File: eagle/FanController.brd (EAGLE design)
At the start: 45 x 20 mm, 16 parts, among them IC102 LDK320AM33R, IC201 STM32F042G6U6, Q302 BSS123

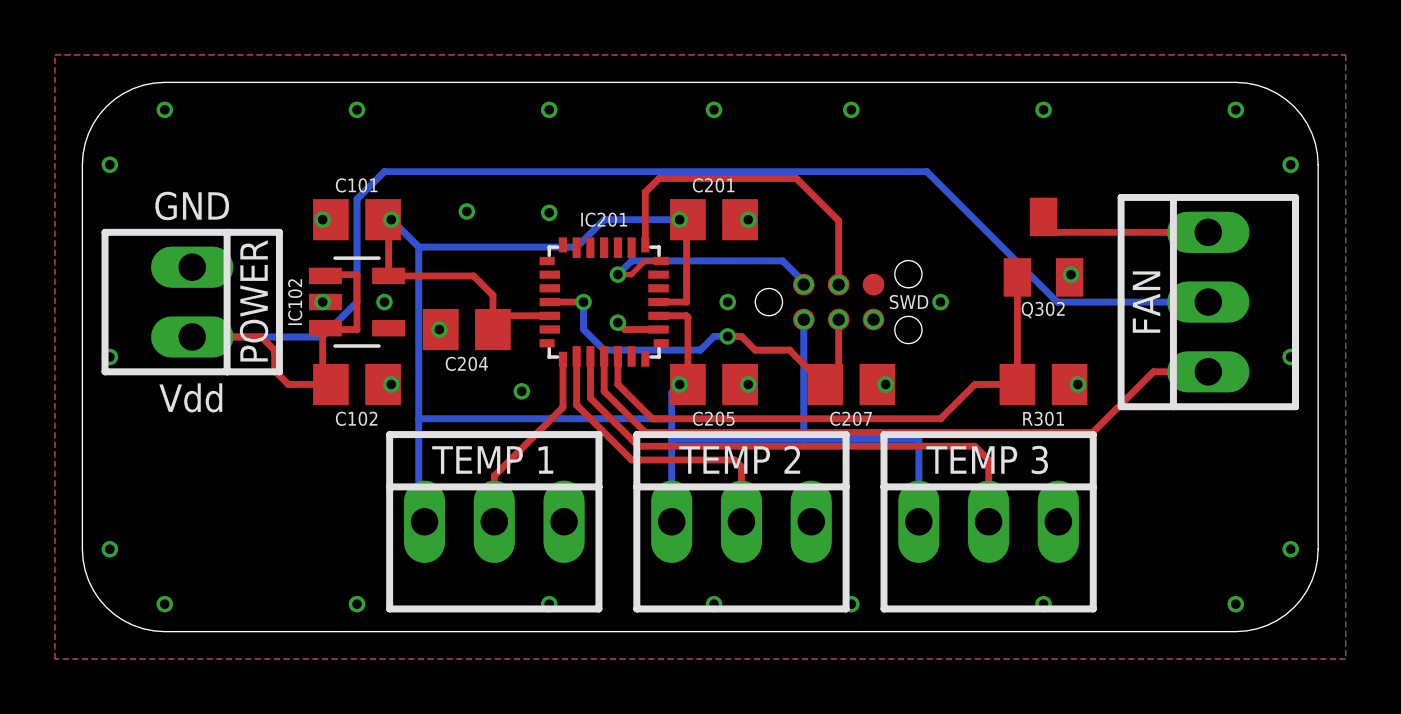
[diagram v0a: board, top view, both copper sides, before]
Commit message: rev.2: PWM fan
- initialized all unused pins as analog
- replaced 3-pin fan connector with 4-pin
- removed FET for transistor control
- added noctua PWM specification white paper
- rev.2 board marking on tstop
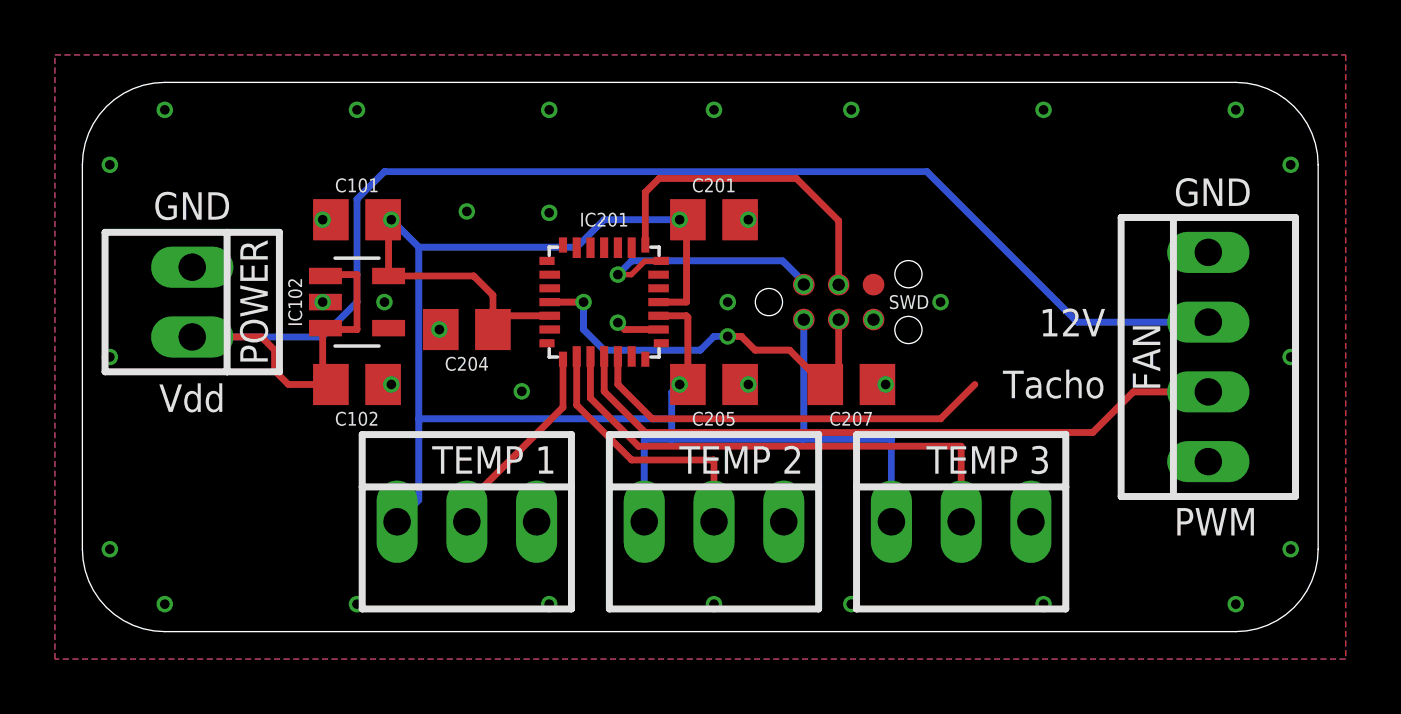
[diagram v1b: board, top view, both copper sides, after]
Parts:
- removed FAN_300: 22-23-2031, con-molex:22-23-2031
- removed Q302: BSS123, transistor-small-signal:SOT23
- removed R301: 10k, rcl:R0805
- added FAN_301: 47053-1000, con-molex:22-23-2041
- moved TEMP400 1.00 mm to (14.0, 4.00)
- moved TEMP500 1.00 mm to (23.0, 4.00)
- moved TEMP600 1.00 mm to (32.0, 4.00)
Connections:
- removed net FAN:N$1: FAN_300.3, Q302.3
- net FAN_PWM: now also FAN_301.1; no longer Q302.1, R301.2
- net FAN_TACHO: now also FAN_301.2; no longer FAN_300.1
- net GND: now also FAN_301.4; no longer Q302.2, R301.1
- net VDD: now also FAN_301.3; no longer FAN_300.2
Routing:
- net FAN:N$1: track 6.56 -> 0.00 mm
- net FAN_PWM: track 20.5 -> 15.1 mm
- net TEMP2: track 10.7 -> 9.85 mm
- net TEMP3: track 19.2 -> 18.5 mm
- net GND: vias 37 -> 35
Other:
- board text added: "12V"
- board text added: "PWM"
- board text added: "Tacho"
- board text added: "ejovrh rev. 2"
- board text removed: "ejovrh rev. 1"

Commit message: - replaced fan connector with pinhead (fan will be soldered)
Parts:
- removed FAN_301: 47053-1000, con-molex:22-23-2041
- added SV301: (no value), con-lstb:MA04-1
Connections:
- net FAN_PWM: now also SV301.3; no longer FAN_301.1
- net FAN_TACHO: now also SV301.2; no longer FAN_301.2
- net GND: now also SV301.1; no longer FAN_301.4
- net VDD: now also SV301.4; no longer FAN_301.3
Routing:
- net FAN_PWM: track 15.1 -> 24.5 mm
- net VDD: track 56.8 -> 55.7 mm
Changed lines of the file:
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@@
 <text x="24" y="6.25" size="1" layer="21" align="center">TEMP 2</text>
 <text x="33" y="6.25" size="1" layer="21" align="center">TEMP 3</text>
-<text x="38.75" y="10" size="1" layer="21" rot="R90" align="center">FAN</text>
+<text x="41" y="3" size="1" layer="21" rot="R180" align="center">FAN</text>
 <text x="6.25" y="12" size="1" layer="21" rot="R90" align="center">POWER</text>
-<text x="39.75" y="16" size="1" layer="21" align="center-left">GND</text>
-<text x="37.25" y="11.25" size="1" layer="21" rot="R180" align="center-left">12V</text>
-<text x="37.25" y="9" size="1" layer="21" rot="R180" align="center-left">Tacho</text>
-<text x="39.75" y="4" size="1" layer="21" align="center-left">PWM</text>
+<text x="39" y="6" size="1" layer="21" rot="R180" align="center-left">GND</text>
+<text x="39" y="13.75" size="1" layer="21" rot="R180" align="center-left">12V</text>
+<text x="39" y="8.75" size="1" layer="21" rot="R180" align="center-left">Tacho</text>
+<text x="39" y="11.25" size="1" layer="21" rot="R180" align="center-left">PWM</text>
 </plain>
 <attributes>
@@
 <attribute name="VALUE" x="-1.08" y="14.54" size="1.016" layer="27" ratio="10" rot="R270"/>
 </element>
-<element name="FAN_301" library="con-molex" library_urn="urn:adsk.eagle:library:165" package="22-23-2041" package3d_urn="urn:adsk.eagle:package:8078635/1" value="47053-1000" x="41" y="10" smashed="yes" rot="R90">
-<attribute name="MF" value="MOLEX" x="41" y="10" size="1.778" layer="27" rot="R90" display="off"/>
-<attribute name="MPN" value="22-23-2041" x="41" y="10" size="1.778" layer="27" rot="R90" display="off"/>
-<attribute name="OC_FARNELL" value="1462920" x="41" y="10" size="1.778" layer="27" rot="R90" display="off"/>
-<attribute name="OC_NEWARK" value="38C0355" x="41" y="10" size="1.778" layer="27" rot="R90" display="off"/>
-<attribute name="POPULARITY" value="21" x="41" y="10" size="1.778" layer="27" rot="R90" display="off"/>
-<attribute name="VALUE" x="46.08" y="4.92" size="1.016" layer="27" ratio="10" rot="R90"/>
+<element name="SV301" library="con-lstb" library_urn="urn:adsk.eagle:library:162" package="MA04-1" package3d_urn="urn:adsk.eagle:package:8337/1" value="" x="41" y="10" smashed="yes" rot="R90">
+<attribute name="MF" value="" x="41" y="10" size="1.778" layer="27" rot="R90" display="off"/>
+<attribute name="MPN" value="" x="41" y="10" size="1.778" layer="27" rot="R90" display="off"/>
+<attribute name="OC_FARNELL" value="unknown" x="41" y="10" size="1.778" layer="27" rot="R90" display="off"/>
+<attribute name="OC_NEWARK" value="unknown" x="41" y="10" size="1.778" layer="27" rot="R90" display="off"/>
+<attribute name="POPULARITY" value="41" x="41" y="10" size="1.778" layer="27" rot="R90" display="off"/>
+<attribute name="VALUE" x="39.349" y="10.635" size="1.27" layer="27" ratio="10" rot="R90"/>
 </element>
 </elements>
@@
 <via x="31.25" y="12" extent="1-16" drill="0.35"/>
 <via x="11" y="12" extent="1-16" drill="0.35"/>
-<contactref element="FAN_301" pad="4"/>
+<contactref element="SV301" pad="1"/>
 <wire x1="44" y1="17" x2="42" y2="19" width="0" layer="19" extent="1-1"/>
-<wire x1="41" y1="13.81" x2="44" y2="17" width="0" layer="19" extent="1-1"/>
-<wire x1="44" y1="10" x2="41" y2="13.81" width="0" layer="19" extent="1-1"/>
+<wire x1="44" y1="10" x2="44" y2="17" width="0" layer="19" extent="1-1"/>
 <wire x1="35" y1="19" x2="42" y2="19" width="0" layer="19" extent="1-1"/>
 <wire x1="44" y1="3" x2="44" y2="10" width="0" layer="19" extent="1-1"/>
@@
 <wire x1="1" y1="3" x2="1" y2="10" width="0" layer="19" extent="1-1"/>
 <wire x1="3" y1="1" x2="1" y2="3" width="0" layer="19" extent="1-1"/>
+<wire x1="41" y1="6.19" x2="44" y2="3" width="0" layer="19" extent="1-1"/>
 </signal>
 <signal name="3V3" class="4">
@@
 <wire x1="4" y1="10.73" x2="6.52" y2="10.73" width="0.25" layer="1"/>
 <wire x1="7.5" y1="9" x2="7" y2="9.5" width="0.25" layer="1"/>
-<wire x1="30.75" y1="16.75" x2="35.25" y2="12.25" width="0.25" layer="16"/>
-<wire x1="35.25" y1="12.25" x2="35.5" y2="12" width="0.25" layer="16"/>
+<wire x1="30.75" y1="16.75" x2="33.69" y2="13.81" width="0.25" layer="16"/>
 <wire x1="4" y1="10.73" x2="8.73" y2="10.73" width="0.25" layer="16"/>
 <wire x1="10" y1="12" x2="10" y2="15.75" width="0.25" layer="16"/>
@@
 <wire x1="11" y1="16.75" x2="30.75" y2="16.75" width="0.25" layer="16"/>
 <wire x1="9.05" y1="9" x2="7.5" y2="9" width="0.25" layer="1"/>
-<contactref element="FAN_301" pad="3"/>
-<wire x1="41" y1="11.27" x2="36.23" y2="11.27" width="0.25" layer="16"/>
-<wire x1="36.23" y1="11.27" x2="35.5" y2="12" width="0.25" layer="16"/>
+<contactref element="SV301" pad="4"/>
+<wire x1="41" y1="13.81" x2="33.69" y2="13.81" width="0.25" layer="16"/>
 </signal>
 <signal name="TEMP1" class="1">
@@
 <wire x1="19.5" y1="10.02" x2="19.5" y2="9" width="0.25" layer="1"/>
 <wire x1="19.5" y1="9" x2="20.75" y2="7.75" width="0.25" layer="1"/>
-<wire x1="32.5" y1="9" x2="31.25" y2="7.75" width="0.25" layer="1"/>
 <wire x1="20.75" y1="7.75" x2="31.25" y2="7.75" width="0.25" layer="1"/>
-<contactref element="FAN_301" pad="1"/>
-<wire x1="41" y1="6.19" x2="19.5" y2="10.02" width="0" layer="19" extent="1-1"/>
+<contactref element="SV301" pad="3"/>
+<wire x1="41" y1="11.27" x2="34.77" y2="11.27" width="0.25" layer="1"/>
+<wire x1="34.77" y1="11.27" x2="31.25" y2="7.75" width="0.25" layer="1"/>
 </signal>
 <signal name="FAN_TACHO" class="1">
@@
 <wire x1="19" y1="8.75" x2="20.5" y2="7.25" width="0.25" layer="1"/>
 <wire x1="20.5" y1="7.25" x2="36.79" y2="7.25" width="0.25" layer="1"/>
-<contactref element="FAN_301" pad="2"/>
-<wire x1="37.645" y1="8.105" x2="36.79" y2="7.25" width="0.25" layer="1"/>
+<contactref element="SV301" pad="2"/>
 <wire x1="41" y1="8.73" x2="38.27" y2="8.73" width="0.25" layer="1"/>
-<wire x1="38.27" y1="8.73" x2="37.645" y2="8.105" width="0.25" layer="1"/>
+<wire x1="38.27" y1="8.73" x2="36.79" y2="7.25" width="0.25" layer="1"/>
 </signal>
 </signals>
